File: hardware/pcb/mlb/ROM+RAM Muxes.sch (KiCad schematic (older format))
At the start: 34 parts, among them Y2 Oscilator

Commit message: Fix typos ADB, PAL16L8D.
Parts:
- UH7: value PAL16L80 -> PAL16L8D; symbol Macintosh_SE_30_Components:PAL16L80 -> Macintosh_SE_30_Components:PAL16L8D
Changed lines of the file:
@@
 $EndComp
 $Comp
-L Macintosh_SE_30_Components:PAL16L80 UH7
+L Macintosh_SE_30_Components:PAL16L8D UH7
 U 1 1 5EBDFEA4
 P 12750 7700
 F 0 "UH7" H 12700 7850 50  0000 C CNN
-F 1 "PAL16L80" H 12700 7750 50  0000 C CNN
+F 1 "PAL16L8D" H 12700 7750 50  0000 C CNN
 F 2 "" H 12750 7700 50  0001 C CNN
 F 3 "" H 12750 7700 50  0001 C CNN

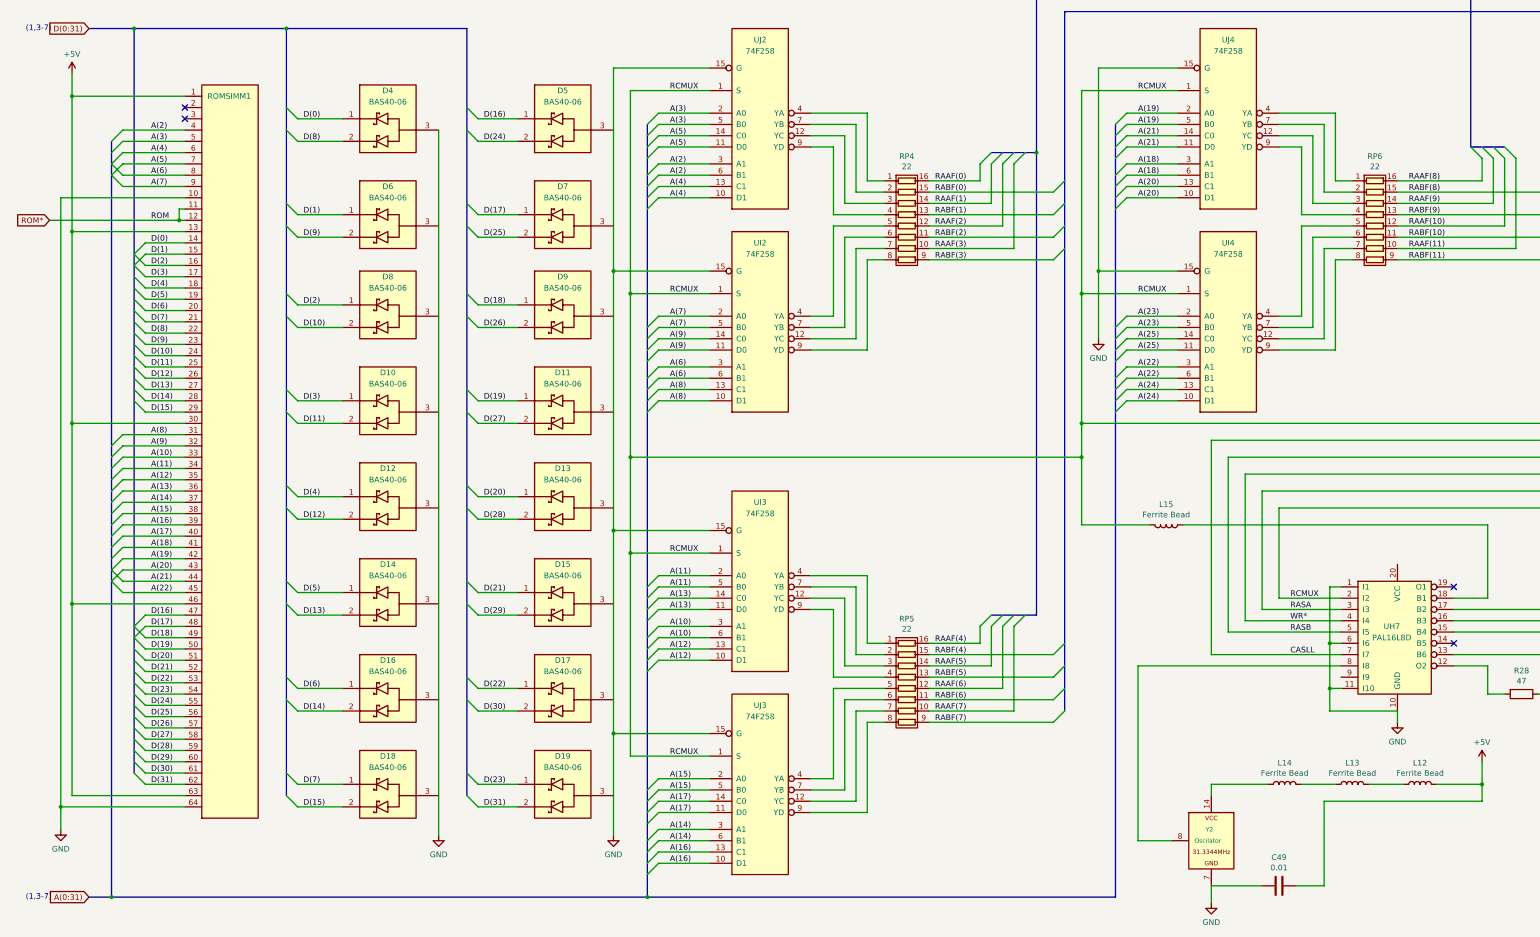
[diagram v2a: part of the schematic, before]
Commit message: Fix errors found in review of the Macintosh SE/30 schematic redraw.
Page 1:

* DSACK*(0:1) (syntax)
* R-W* (inconsistent syntax)
* IPL different syntax
* PDS 38, C16M not grounded
* PDS 39, should be grounded

Page 2:

* RAAF*(8), RABF*(9), RAAF*(10), RABF*(10) (syntax)
* RCMUX* (syntax)
* ROM* missing page 3 indicator
* ROMSIMM1 GND 10, 30, 64
* ROMSIMM1 Incorrect +5V lines
* ROMSIMM1 Confusing bus line drawing angles makes connections look
  duplicated

Page 3:

* VIAIRQ2* (syntax)
* VIAIRQ1N (syntax, on GLUE template)
* SCCRD* (syntax)

Page 4:

* VIA template, RS0, RS1, RS2, RS3 erroneously written as R50, R51,
  R52, R53
* V1PB7 erroneously written as VIPB7
* RTC-D erroneously written as RTC-O
* V1PA0, V1PA1, V1PA2 erroneously written as VIPA0, VIPA1, VIPA2
* warning: additional label BATT not present
* UL11 ADB template, P5 erroneously written as P2
* ADBO erroneously written as ADB0
* SNDINT* erroneously written as SNTINT*

Page 5:

* HSYNC* on UG7 (syntax)
* UJ6 confusing bus line makes signals look duplicated
* Video ROM UK6 not labeled with reference designator (already inside
  KiCad file, stale PDF?)
* VIDS4, VIDS3, VIDS2, VIDS1, VIDS0 erroneously written a VID54,
  VID53, VID53, VID51, VID50
* R-W* alternate page reference erroneously written as RW*
* 74F253 template, G erroneously labeled as GND
* 74F253 template, missing second G enable pin
* style: C0 in 74F253 template should not be C0(GND)
* warning: UA8 ALTVID line could have another label close to the chip

Page 6:

* warning: On SWIM, WRDATA could have label WR*
* DB25 connector: DP*, DB0*, DB1*, DB2*, DB3*, DB4*, DB5*, DB6*, DB7*
  (syntax)
* J8 Ribbon Connector: Missing +12V on 13, 15, 17, 19
* J6 DB-19: Missing +12V-DSK on 7, 8
* warning: missing RDDATA.F additional label near J6 DB-19 pin 18
* warning: missing WRITE.F additional label near J6 DB-19 pin 19
* warning: confusing bus line layout on 53C80 looks like duplicate
  wiring

Page 7:

* RXDA+ erroneously written as RXDB+
* HSKOA erroneo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
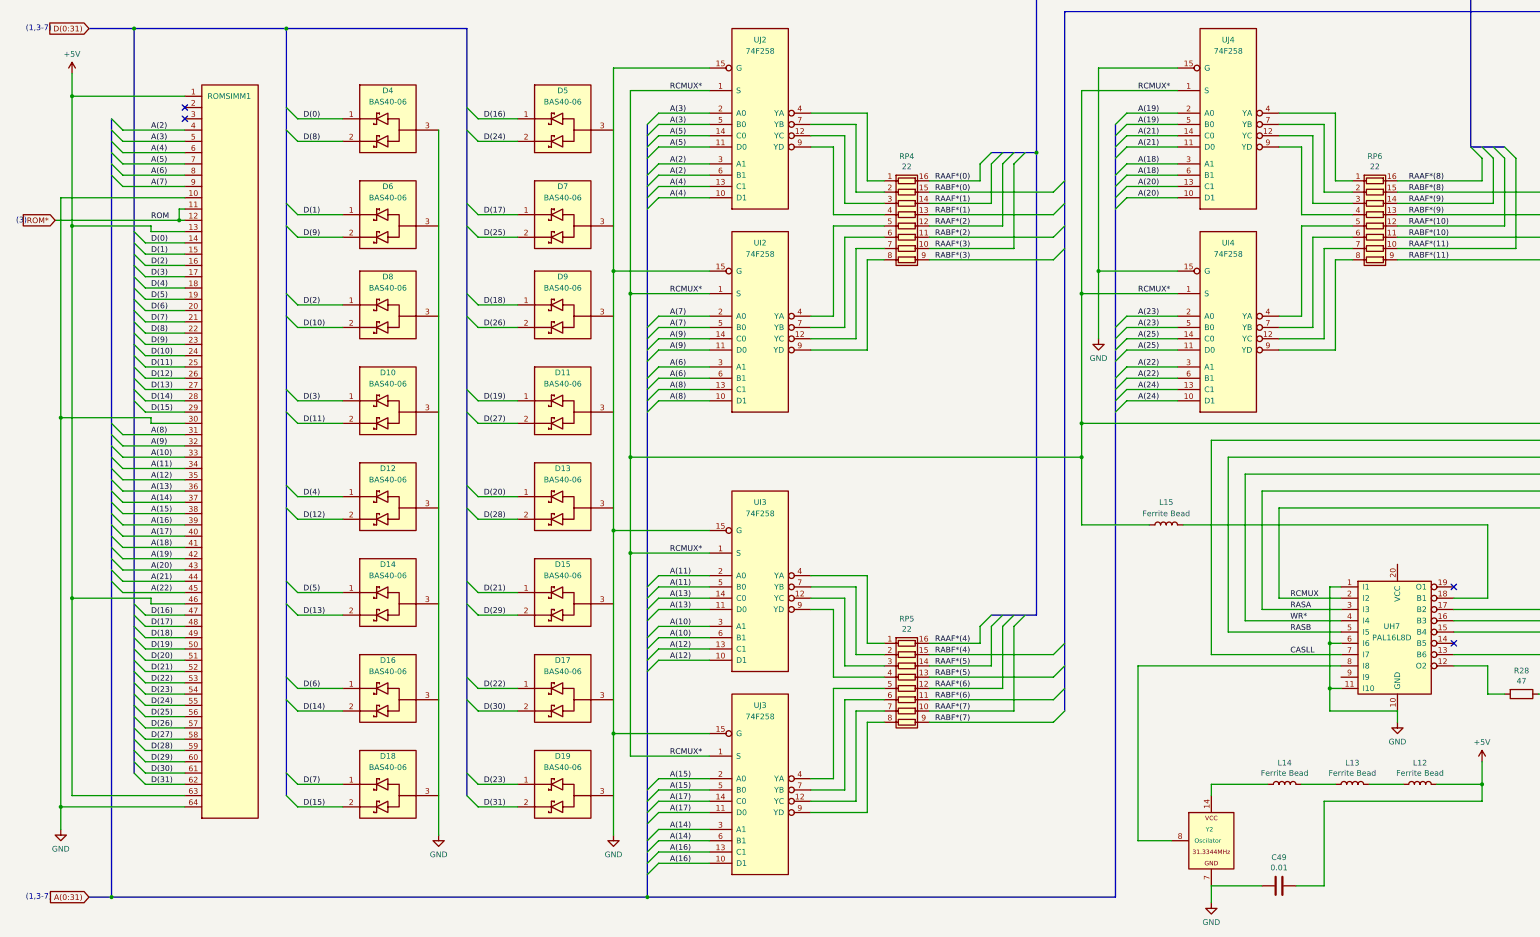
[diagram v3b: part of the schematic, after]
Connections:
- net +5V: no longer ROMSIMM1.30
- net GND: now also ROMSIMM1.30
- net RCMUX: no longer L15.2, UI2.1 (S), UI3.1 (S), UI4.1 (S), UJ2.1 (S), UJ3.1 (S), UJ4.1 (S)
- net at UH7.18 (B1): now also L15.2; no longer L15.1
- net RAAF(0) renamed RAAF*(0)
- net RAAF(1) renamed RAAF*(1)
- net RAAF(10) renamed RAAF*(10)
- net RAAF(11) renamed RAAF*(11)
- net RAAF(2) renamed RAAF*(2)
- net RAAF(3) renamed RAAF*(3)
- net RAAF(4) renamed RAAF*(4)
- net RAAF(5) renamed RAAF*(5)
- net RAAF(6) renamed RAAF*(6)
- net RAAF(7) renamed RAAF*(7)
- net RAAF(8) renamed RAAF*(8)
- net RAAF(9) renamed RAAF*(9)
- net RABF(0) renamed RABF*(0)
- net RABF(1) renamed RABF*(1)
- net RABF(10) renamed RABF*(10)
- net RABF(11) renamed RABF*(11)
- net RABF(2) renamed RABF*(2)
- net RABF(3) renamed RABF*(3)
- net RABF(4) renamed RABF*(4)
- net RABF(5) renamed RABF*(5)
- net RABF(6) renamed RABF*(6)
- net RABF(7) renamed RABF*(7)
- net RABF(8) renamed RABF*(8)
- net RABF(9) renamed RABF*(9)
- new net RCMUX*: L15.1, UI2.1 (S), UI3.1 (S), UI4.1 (S), UJ2.1 (S), UJ3.1 (S), UJ4.1 (S)
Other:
- moved on the sheet: L15
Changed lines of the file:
@@
 	2000 2850 1000 2850
 Wire Wire Line
-	1000 2850 1000 4050
-Wire Wire Line
 	1000 9050 2000 9050
 Wire Wire Line
 	900  9150 2000 9150
-Connection ~ 1000 4050
 NoConn ~ 2000 2950
 NoConn ~ 2000 3050
 Wire Wire Line
 	2000 3850 1950 3850
-Text GLabel 800  3950 0    50   Input ~ 0
+Text GLabel 850  3950 0    50   Input ~ 0
 ROM*
 Wire Wire Line
@@
 Connection ~ 5950 6900
 Text Label 6300 2800 0    50   ~ 0
-RCMUX
+RCMUX*
 Wire Wire Line
 	6650 7100 6200 7100
@@
 	6650 9550 6200 9550
 Text Label 6300 6900 0    50   ~ 0
-RCMUX
+RCMUX*
 Text Label 6300 7100 0    50   ~ 0
 A(11)
@@
 A(12)
 Text Label 6300 8700 0    50   ~ 0
-RCMUX
+RCMUX*
 Text Label 6300 8900 0    50   ~ 0
 A(15)
@@
 RCMUX*
 Text Label 10450 2800 0    50   ~ 0
-RCMUX
+RCMUX*
 Text Label 10450 4600 0    50   ~ 0
-RCMUX
+RCMUX*
 Text Label 10450 5550 0    50   ~ 0
 A(24)
@@
 	8600 7700 9050 7700
 Text Label 8650 3600 0    50   ~ 0
-RAAF(0)
+RAAF*(0)
 Text Label 8650 3800 0    50   ~ 0
-RAAF(1)
+RAAF*(1)
 Text Label 8650 4000 0    50   ~ 0
-RAAF(2)
+RAAF*(2)
 Text Label 8650 4200 0    50   ~ 0
-RAAF(3)
+RAAF*(3)
 Text Label 8650 7700 0    50   ~ 0
-RAAF(4)
+RAAF*(4)
 Text Label 8650 7900 0    50   ~ 0
-RAAF(5)
+RAAF*(5)
 Text Label 8650 8100 0    50   ~ 0
-RAAF(6)
+RAAF*(6)
 Text Label 8650 8300 0    50   ~ 0
-RAAF(7)
+RAAF*(7)
 Text Label 8650 3700 0    50   ~ 0
-RABF(0)
+RABF*(0)
 Text Label 8650 3900 0    50   ~ 0
-RABF(1)
+RABF*(1)
 Text Label 8650 4100 0    50   ~ 0
-RABF(2)
+RABF*(2)
 Text Label 8650 4300 0    50   ~ 0
-RABF(3)
+RABF*(3)
 Text Label 8650 7800 0    50   ~ 0
-RABF(4)
+RABF*(4)
 Text Label 8650 8000 0    50   ~ 0
-RABF(5)
+RABF*(5)
 Text Label 8650 8200 0    50   ~ 0
-RABF(6)
+RABF*(6)
 Text Label 8650 8400 0    50   ~ 0
-RABF(7)
+RABF*(7)
 Text GLabel 15800 1900 2    50   Input ~ 0
 RAAF*(0:11)
@@
 	12750 3600 13500 3600
 Text Label 12850 3600 0    50   ~ 0
-RAAF(8)
+RAAF*(8)
 Text Label 12850 3800 0    50   ~ 0
-RAAF(9)
+RAAF*(9)
 Text Label 12850 4000 0    50   ~ 0
-RAAF(10)
+RAAF*(10)
 Text Label 12850 4200 0    50   ~ 0
-RAAF(11)
+RAAF*(11)
 Text Label 12850 3700 0    50   ~ 0
-RABF(8)
+RABF*(8)
 Text Label 12850 3900 0    50   ~ 0
-RABF(9)
+RABF*(9)
 Text Label 12850 4100 0    50   ~ 0
-RABF(10)
+RABF*(10)
 Text Label 12850 4300 0    50   ~ 0
-RABF(11)
+RABF*(11)
 Text GLabel 15800 5900 2    50   Input ~ 0
 CASLL
@@
 U 1 1 5FCCA01E
 P 10700 6650
-F 0 "L15" V 10519 6650 50  0000 C CNN
-F 1 "Ferrite Bead" V 10610 6650 50  0000 C CNN
+F 0 "L15" V 10900 6650 50  0000 C CNN
+F 1 "Ferrite Bead" V 10800 6650 50  0000 C CNN
 F 2 "" H 10700 6650 50  0001 C CNN
 F 3 "~" H 10700 6650 50  0001 C CNN
 	1    10700 6650
-	0    1    1    0
+	0    -1   -1   0
 $EndComp
 Wire Wire Line
@@
 D(31)
 Entry Wire Line
-	1650 7450 1550 7550
-Entry Wire Line
-	1650 7550 1550 7650
+	1650 7450 1550 7350
+Entry Wire Line
+	1650 7550 1550 7450
 Entry Wire Line
 	1650 7650 1550 7550
@@
 	1650 8950 1550 8850
 Entry Wire Line
-	1650 5650 1550 5550
-Entry Wire Line
-	1650 5550 1550 5450
-Entry Wire Line
-	1650 5450 1550 5350
-Entry Wire Line
-	1650 5350 1550 5250
-Entry Wire Line
-	1650 5250 1550 5150
-Entry Wire Line
-	1650 5150 1550 5050
-Entry Wire Line
 	1650 5050 1550 4950
 Entry Wire Line
@@
 Entry Wire Line
 	1650 4450 1550 4350
-Entry Wire Line
-	1650 4350 1550 4250
-Wire Wire Line
-	1000 4050 1000 5750
-Connection ~ 1000 5750
 Entry Wire Line
 	3000 3050 2900 2950
@@
 Wire Bus Line
 	2900 2250 1550 2250
-Entry Wire Line
-	1450 3650 1350 3550
-Entry Wire Line
-	1450 3450 1350 3550
-Entry Wire Line
-	1450 3350 1350 3450
-Entry Wire Line
-	1450 3250 1350 3350
-Entry Wire Line
-	1450 3150 1350 3250
-Wire Wire Line
-	800  3950 1950 3950
+Wire Wire Line
+	850  3950 1950 3950
 Connection ~ 1950 3950
 Entry Wire Line
-	1450 5850 1350 5950
-Entry Wire Line
-	1450 5950 1350 6050
-Entry Wire Line
-	1450 6050 1350 6150
-Entry Wire Line
-	1450 6150 1350 6250
-Entry Wire Line
-	1450 6250 1350 6350
-Entry Wire Line
-	1450 6350 1350 6450
-Entry Wire Line
-	1450 6450 1350 6550
-Entry Wire Line
-	1450 6550 1350 6650
-Entry Wire Line
-	1450 6650 1350 6750
-Entry Wire Line
-	1450 6750 1350 6850
-Entry Wire Line
-	1450 6850 1350 6950
-Entry Wire Line
-	1450 6950 1350 7050
-Entry Wire Line
-	1450 7050 1350 7150
-Wire Wire Line
-	1000 5750 1000 7350
-Connection ~ 1000 7350
-Wire Wire Line
-	1000 7350 1000 9050
-Wire Wire Line
-	1000 5750 2000 5750
+	1450 5850 1350 5750
+Entry Wire Line
+	1450 5950 1350 5850
+Entry Wire Line
+	1450 6050 1350 5950
+Entry Wire Line
+	1450 6150 1350 6050
+Entry Wire Line
+	1450 6250 1350 6150
+Entry Wire Line
+	1450 6350 1350 6250
+Entry Wire Line
+	1450 6450 1350 6350
+Entry Wire Line
+	1450 6550 1350 6450
+Entry Wire Line
+	1450 6650 1350 6550
+Entry Wire Line
+	1450 6750 1350 6650
+Entry Wire Line
+	1450 6850 1350 6750
+Entry Wire Line
+	1450 6950 1350 6850
+Entry Wire Line
+	1450 7050 1350 6950
 Wire Bus Line
 	1350 9950 1150 9950
@@
 	6650 3000 6200 3000
 Text Label 6300 4600 0    50   ~ 0
-RCMUX
+RCMUX*
 Text Label 6300 5550 0    50   ~ 0
 A(8)
@@
 Text Notes 820  2280 2    50   ~ 0
 (1,3-7)
-Wire Wire Line
-	1000 4050 2000 4050
-Entry Wire Line
-	1650 4250 1550 4350
-Entry Wire Line
-	1650 4150 1550 4250
+Entry Wire Line
+	1450 7250 1350 7150
+Wire Wire Line
+	900  3750 2000 3750
+Text Notes 600  3984 2    50   ~ 0
+(3)
+Entry Wire Line
+	1450 3650 1350 3550
+Entry Wire Line
+	1450 3550 1350 3450
+Entry Wire Line
+	1450 3450 1350 3350
+Entry Wire Line
+	1450 3350 1350 3250
+Entry Wire Line
+	1450 3250 1350 3150
+Entry Wire Line
+	1450 3150 1350 3050
+Entry Wire Line
+	1650 4150 1550 4050
+Entry Wire Line
+	1650 5150 1550 5050
+Entry Wire Line
+	1650 5250 1550 5150
+Entry Wire Line
+	1650 5350 1550 5250
+Entry Wire Line
+	1650 5450 1550 5350
+Entry Wire Line
+	1650 5550 1550 5450
+Entry Wire Line
+	1650 5650 1550 5550
+Entry Wire Line
+	1650 4250 1550 4150
+Wire Wire Line
+	2000 4050 1700 4050
+Wire Wire Line
+	1700 4050 1700 4000
+Entry Wire Line
+	1650 4350 1550 4250
+Wire Wire Line
+	1000 2850 1000 4000
+Wire Wire Line
+	2000 7350 1700 7350
+Wire Wire Line
+	1700 7350 1700 7300
+Wire Wire Line
+	1700 7300 1000 7300
+Connection ~ 1000 7300
+Wire Wire Line
+	1000 7300 1000 9050
+Wire Wire Line
+	1700 4000 1000 4000
+Connection ~ 1000 4000
+Wire Wire Line
+	1000 4000 1000 7300
+Wire Wire Line
+	900  3750 900  5700
+Wire Wire Line
+	2000 5750 1700 5750
+Wire Wire Line
+	1700 5750 1700 5700
+Wire Wire Line
+	1700 5700 900  5700
+Connection ~ 900  5700
+Wire Wire Line
+	900  5700 900  9150
 Entry Wire Line
 	1450 7150 1350 7050
-Entry Wire Line
-	1450 7250 1350 7150
-Wire Wire Line
-	1000 7350 2000 7350
-Entry Wire Line
-	1450 3550 1350 3450
-Wire Wire Line
-	900  3750 900  9150
-Wire Wire Line
-	900  3750 2000 3750
 Wire Bus Line
 	13400 3300 13700 3300
@@
 	14350 3300 14650 3300
 Wire Bus Line
+	9150 7450 9550 7450
+Wire Bus Line
 	9150 3350 9550 3350
 Wire Bus Line
-	9150 7450 9550 7450
-Wire Bus Line
 	9800 2100 9800 8300
 Wire Bus Line
+	1350 3050 1350 9950
+Wire Bus Line
 	10250 3100 10250 9950
 Wire Bus Line
-	1350 3250 1350 9950
-Wire Bus Line
 	4500 2250 4500 9050
